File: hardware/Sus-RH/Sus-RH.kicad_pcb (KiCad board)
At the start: 2 copper layers, 43.5 x 61.2 mm, 47 parts, among them J1 Conn_01x06, J2 Conn_01x05, J3 Conn_01x05, J4 Conn_01x05, J5 Conn_01x06, J6 Conn_01x03, J7 53307-2471, U1 TLV9002QDRQ1

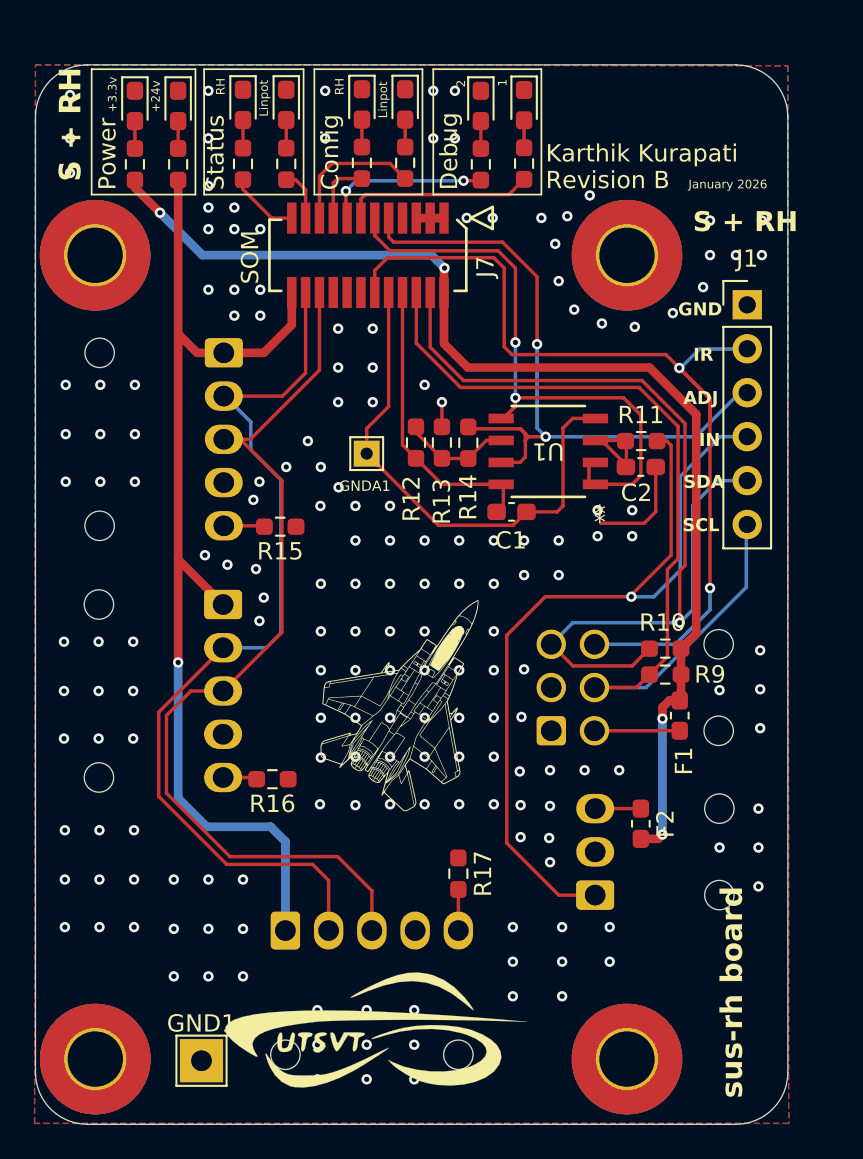
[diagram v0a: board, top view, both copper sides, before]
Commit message: fixed nanofit for linpot
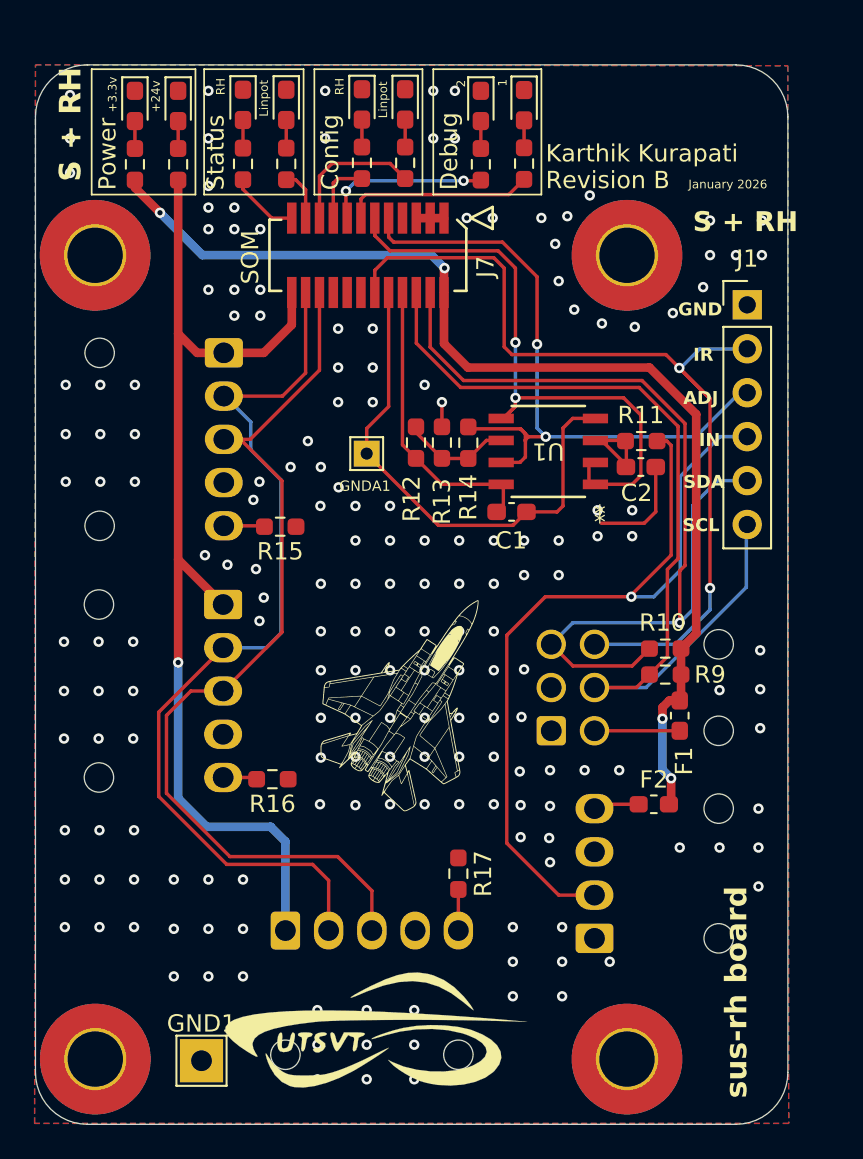
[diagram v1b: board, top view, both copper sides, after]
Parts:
- J6: value Conn_01x03 -> Conn_01x04; footprint Connector_Molex:Molex_Nano-Fit_105313-xx03_1x03_P2.50mm_Horizontal -> Connector_Molex:Molex_Nano-Fit_105313-xx04_1x04_P2.50mm_Horizontal
- moved J6 2.50 mm to (136.6, 90.8)
- moved F2 1.35 mm to (140.0, 83.0), turned to 0 degrees
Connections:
- F2 pad 1: Net-(J6-Pin_3) -> Net-(J6-Pin_4)
- J6 pad 1: /linpot_in -> GND
- J6 pad 2: GND -> /linpot_in
- J6 pad 3: Net-(J6-Pin_3) -> GND
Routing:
- net +3.3V: track 67.7 -> 64.9 mm
- net Net-(J6-Pin_3): track 2.64 -> 0.00 mm
- net Net-(J6-Pin_4): track 0.00 -> 2.31 mm
- net /IR_INTER: track 55.1 -> 53.6 mm
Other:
- board text added: "3.3v"
- board text added: "INT"

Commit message: added "validated silkscreen"
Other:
- board text added: "validated"
